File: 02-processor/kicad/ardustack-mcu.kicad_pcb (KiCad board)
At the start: 2 copper layers, 68.6 x 53.3 mm, 15 parts, among them J1 1-2199298-9, P1 Power, P2 Analog, P3 Digital, P4 Digital, P5 CONN_01X01, P6 CONN_01X01, P7 CONN_01X01, P8 CONN_01X01, Y1 ABL-16.000MHZ-B2

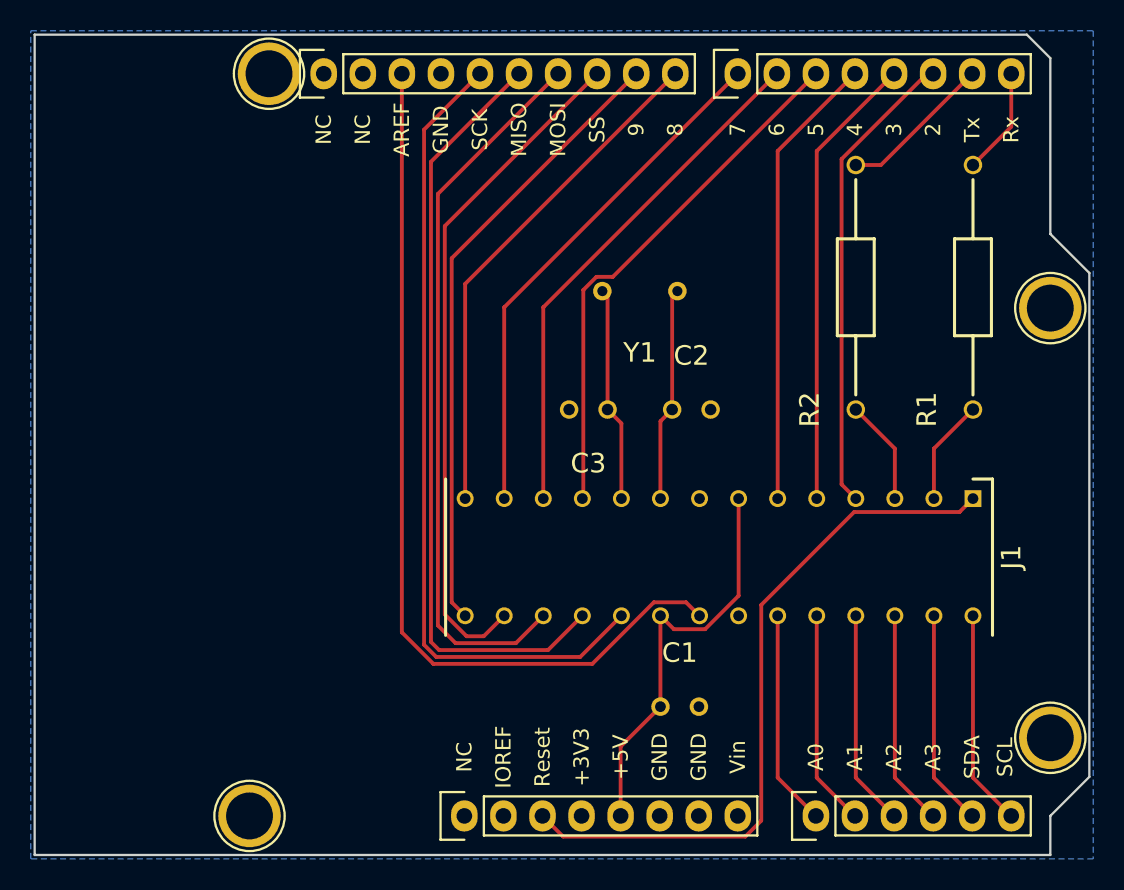
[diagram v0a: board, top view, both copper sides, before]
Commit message: Updates Ardustack microcontroller board PCB silkscreen
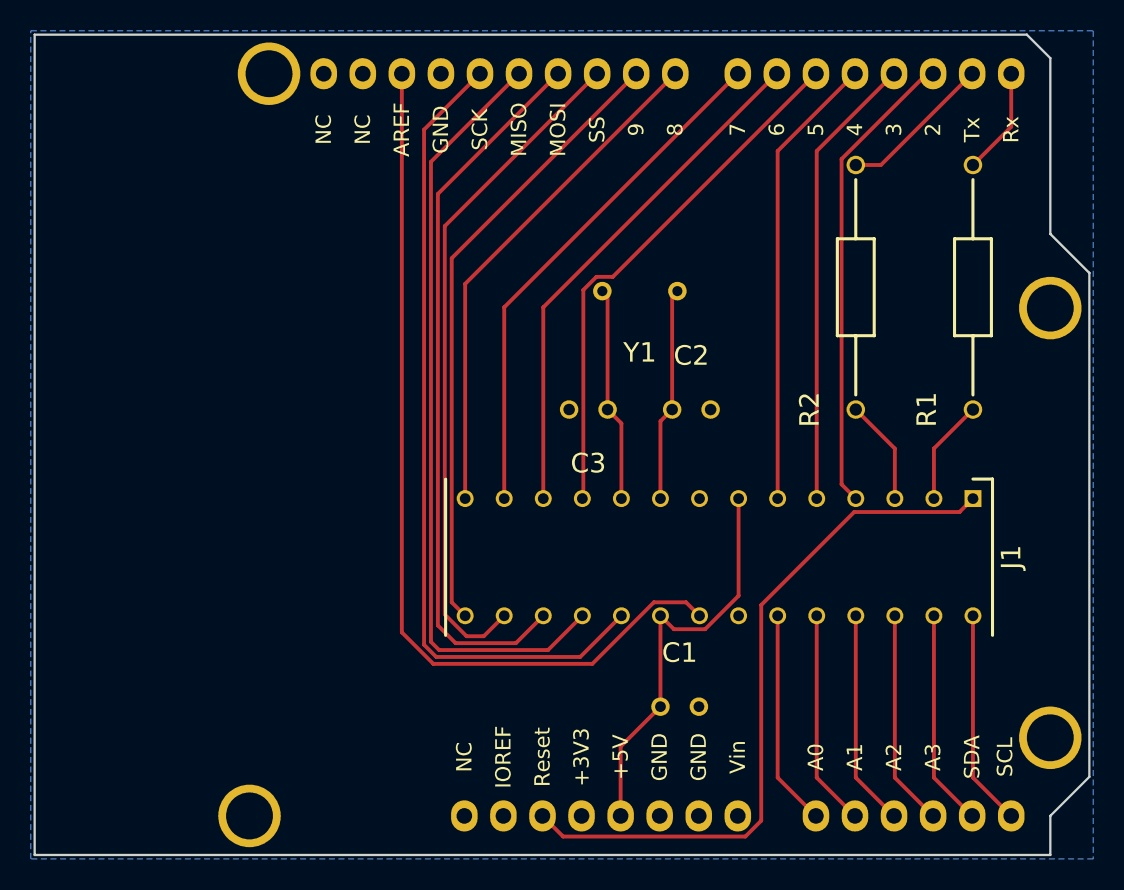
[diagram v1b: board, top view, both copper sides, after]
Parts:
- added G***: LOGO, ardustack-mcu:emblem, B.Cu at (123.8, 108.8)
- added G***: LOGO, ardustack-mcu:name_plate, B.Cu at (123.8, 88.8)

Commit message: Updates PCBs with name and version
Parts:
- moved G*** 0.60 mm to (123.8, 89.4)
- moved G*** 0.20 mm to (123.8, 109.0)
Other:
- board text added: "ARDUSTACK MCU PCB v0.9.0"
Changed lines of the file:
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@@
   )
   (footprint "ardustack-mcu:emblem" (layer "B.Cu")
-    (at 123.8 108.8 180)
+    (at 123.8 109 180)
     (attr board_only exclude_from_pos_files exclude_from_bom)
     (fp_text reference "G***" (at 0 0) (layer "B.SilkS") hide
@@
   )
   (footprint "ardustack-mcu:name_plate" (layer "B.Cu")
-    (at 123.8 88.8 180)
+    (at 123.8 89.4 180)
     (attr board_only exclude_from_pos_files exclude_from_bom)
     (fp_text reference "G***" (at 0 0) (layer "B.SilkS") hide
@@
   (gr_line (start 175.514 73.025) (end 110.998 73.025) (layer "Edge.Cuts") (width 0.15))
   (gr_line (start 177.038 85.979) (end 177.038 74.549) (layer "Edge.Cuts") (width 0.15))
+  (gr_text "ARDUSTACK MCU PCB v0.9.0" (at 123.7 81.4) (layer "B.SilkS")
+    (effects (font (size 1 1) (thickness 0.15)) (justify mirror))
+  )
   (gr_text "4" (at 164.338 79.2 90) (layer "F.SilkS")
     (effects (font (size 1 1) (thickness 0.15)))

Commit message: Updates power, processor, and I/O boards to v1.0.0
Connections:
- P1 pad 2: /IOREF -> +5V
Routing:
- net +5V: track 26.7 -> 35.5 mm
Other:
- board text added: "(+3V3)"
- board text added: "(Vin)"
- board text added: "ARDUSTACK MCU PCB v1.0.0"
- board text removed: "+3V3"
- board text removed: "ARDUSTACK MCU PCB v0.9.0"
- board text removed: "Vin"
